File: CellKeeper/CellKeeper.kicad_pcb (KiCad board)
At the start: 4 copper layers, 260 x 113 mm, 470 parts, among them J1 Screw_Terminal_01x04, J10 3.81P Screw Terminal, J11 USB_C_Receptacle_USB2.0_16P, J12 Conn_02x10_Odd_Even, J14 ZE05H-8DP-2H, J15 Screw_Terminal_01x04, J16 Conn_01x03, J17 OEM HV Sense Connector, J18 7.62mm Pitch Screw Terminal, J19 USB_C_Receptacle_USB2.0_16P, J2 Screw_Terminal_01x01, J20 OEM Connector, J21 3.81P Screw Terminal, J22 Conn_02x10_Odd_Even, J3 Screw_Terminal_01x04, J4 8P8C_LED_Shielded_x2, J5 8P8C_LED_Shielded_x2, J6 S44B-RAD1AK, J7 Screw_Terminal_01x04, J8 Conn_01x03, J9 USB_C_Receptacle_USB2.0_16P, Q1 BSC0805LS, Q2 BSC0805LS, Q3 BSC0805LS, Q4 BSC0805LS, SW1 TS-1187A-B-A-B, SW2 TS-1187A-B-A-B, SW3 TS-1187A-B-A-B, SW4 TS-1187A-B-A-B, U1 UCC27524DR, U10 ISO1050DUB, U11 UCC27524DR, U12 LTV-217-B-G, U13 LTV-217-B-G, U14 RP2354B, U15 F0505S-1WR3, U16 ISO1540, U17 INA228, U18 ADS1115, U19 ADS1115, U20 RP2354B, U21 SP3485EN-L/TR, U22 AM26LV32EIDR, U25 TLV1117LV33DCYR, U26 TLV1117LV33DCYR, U3 TPS5430DDAR, U4 F0505S-1WR3, U5 ISO1050DUB, U6 LTV-217-B-G, U7 LTV-217-B-G, U8 LTV-217-B-G, U9 LTV-217-B-G, Y1 ABM8-272-T3, Y2 ABM8-272-T3

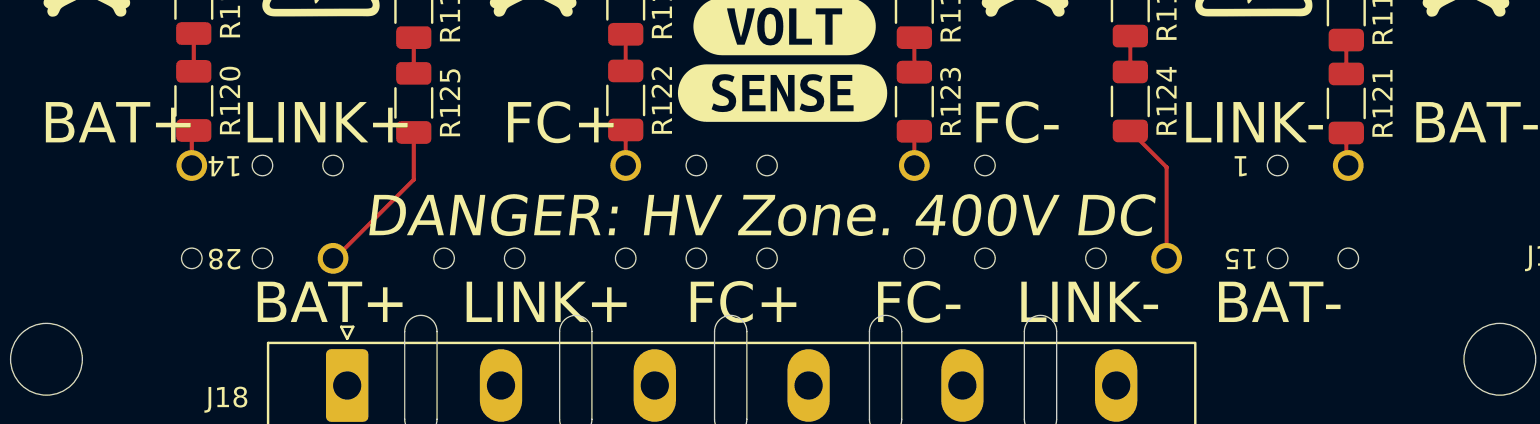
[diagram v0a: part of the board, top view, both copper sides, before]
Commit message: Update Symbol HV Sense
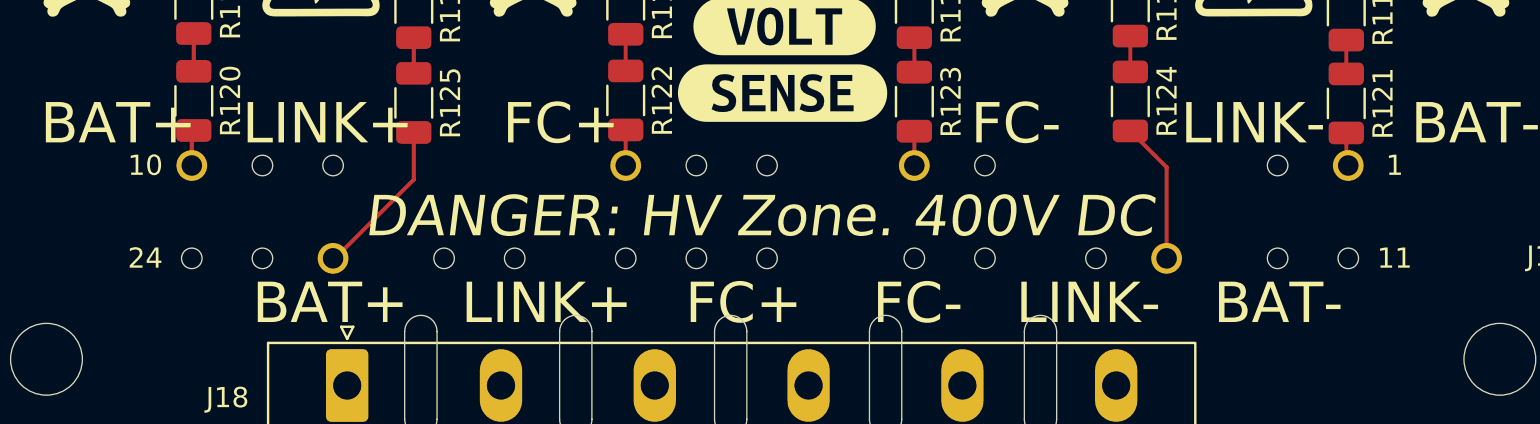
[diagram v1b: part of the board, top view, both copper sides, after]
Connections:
- J17 pad 1: Batt Positive -> Batt Negative
- J17 pad 10: Batt Negative -> Batt Positive
- J17 pad 13: Link Positive -> Link Negative
- J17 pad 22: Link Negative -> Link Positive
- J17 pad 4: FC Positive -> FC Negative
- J17 pad 7: FC Negative -> FC Positive
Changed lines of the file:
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@@
 			)
 		)
-		(property "Description" "Generic connector, single row, 01x24, script generated (kicad-library-utils/schlib/autogen/connector/)"
+		(property "Description" "TE 070 Multilock 24-position right-angle PCB header, TE circuit numbering, pins drawn as on the PCB"
 			(at 0 0 180)
 			(layer "F.Fab")
@@
 			(layer "F.Fab")
 		)
-		(fp_text user "14"
-			(at 4.768898 4.600001 180)
-			(unlocked yes)
-			(layer "F.SilkS")
-			(effects
-				(font
-					(size 1 1)
-					(thickness 0.15)
-				)
-			)
-		)
-		(fp_text user "28"
-			(at 4.768898 0 180)
+		(fp_text user "10"
+			(at 8.7019 4.6 0)
+			(unlocked yes)
+			(layer "F.SilkS")
+			(effects
+				(font
+					(size 1 1)
+					(thickness 0.15)
+				)
+			)
+		)
+		(fp_text user "24"
+			(at 8.7019 0 0)
 			(unlocked yes)
 			(layer "F.SilkS")
@@
 		)
 		(fp_text user "1"
-			(at -45.578298 4.600001 180)
-			(unlocked yes)
-			(layer "F.SilkS")
-			(effects
-				(font
-					(size 1 1)
-					(thickness 0.15)
-				)
-			)
-		)
-		(fp_text user "15"
-			(at -45.578298 0 180)
-			(unlocked yes)
-			(layer "F.SilkS")
-			(effects
-				(font
-					(size 1 1)
-					(thickness 0.15)
-				)
-			)
-		)
-		(fp_text user "14"
-			(at 4.768898 4.600001 0)
+			(at -53.1981 4.6 0)
+			(unlocked yes)
+			(layer "F.SilkS")
+			(effects
+				(font
+					(size 1 1)
+					(thickness 0.15)
+				)
+			)
+		)
+		(fp_text user "11"
+			(at -53.1981 0 0)
+			(unlocked yes)
+			(layer "F.SilkS")
+			(effects
+				(font
+					(size 1 1)
+					(thickness 0.15)
+				)
+			)
+		)
+		(fp_text user "10"
+			(at 8.7019 4.6 0)
 			(unlocked yes)
 			(layer "B.SilkS")
@@
 			)
 		)
-		(fp_text user "28"
-			(at 4.768898 0 0)
+		(fp_text user "24"
+			(at 8.7019 0 0)
 			(unlocked yes)
 			(layer "B.SilkS")
@@
 		)
 		(fp_text user "1"
-			(at -45.578298 4.600001 0)
+			(at -53.1981 4.6 0)
 			(unlocked yes)
 			(layer "B.SilkS")
@@
 			)
 		)
-		(fp_text user "15"
-			(at -45.578298 0 0)
+		(fp_text user "11"
+			(at -53.1981 0 0)
 			(unlocked yes)
 			(layer "B.SilkS")
@@
 			)
 		)
-		(fp_text user "14"
-			(at 4.768898 4.600001 180)
-			(unlocked yes)
-			(layer "F.Fab")
-			(effects
-				(font
-					(size 1 1)
-					(thickness 0.15)
-				)
-			)
-		)
-		(fp_text user "28"
-			(at 4.768898 0 180)
+		(fp_text user "10"
+			(at 8.7019 4.6 0)
+			(unlocked yes)
+			(layer "F.Fab")
+			(effects
+				(font
+					(size 1 1)
+					(thickness 0.15)
+				)
+			)
+		)
+		(fp_text user "24"
+			(at 8.7019 0 0)
 			(unlocked yes)
 			(layer "F.Fab")
@@
 		)
 		(fp_text user "1"
-			(at -45.578298 4.600001 180)
-			(unlocked yes)
-			(layer "F.Fab")
-			(effects
-				(font
-					(size 1 1)
-					(thickness 0.15)
-				)
-			)
-		)
-		(fp_text user "15"
-			(at -45.578298 0 180)
+			(at -53.1981 4.6 0)
+			(unlocked yes)
+			(layer "F.Fab")
+			(effects
+				(font
+					(size 1 1)
+					(thickness 0.15)
+				)
+			)
+		)
+		(fp_text user "11"
+			(at -53.1981 0 0)
 			(unlocked yes)
 			(layer "F.Fab")
@@
 			(layers "*.Cu" "*.Mask")
 		)
+		(pad "10" thru_hole circle
+			(at 6.399322 4.600001 180)
+			(size 1.524 1.524)
+			(drill 1.016)
+			(layers "*.Cu" "*.Mask")
+			(remove_unused_layers no)
+			(net "Batt Positive")
+			(pintype "passive")
+		)
+		(pad "7" thru_hole circle
+			(at -15.1 4.600001 180)
+			(size 1.524 1.524)
+			(drill 1.016)
+			(layers "*.Cu" "*.Mask")
+			(remove_unused_layers no)
+			(net "FC Positive")
+			(pintype "passive")
+		)
+		(pad "4" thru_hole circle
+			(at -29.398782 4.600001 180)
+			(size 1.524 1.524)
+			(drill 1.016)
+			(layers "*.Cu" "*.Mask")
+			(remove_unused_layers no)
+			(net "FC Negative")
+			(pintype "passive")
+		)
 		(pad "1" thru_hole circle
-			(at 6.399322 4.600001 180)
-			(size 1.524 1.524)
-			(drill 1.016)
-			(layers "*.Cu" "*.Mask")
-			(remove_unused_layers no)
-			(net "Batt Positive")
-			(pinfunction "Pin_1_1")
-			(pintype "passive")
-		)
-		(pad "4" thru_hole circle
-			(at -15.1 4.600001 180)
-			(size 1.524 1.524)
-			(drill 1.016)
-			(layers "*.Cu" "*.Mask")
-			(remove_unused_layers no)
-			(net "FC Positive")
-			(pinfunction "Pin_4_4")
-			(pintype "passive")
-		)
-		(pad "7" thru_hole circle
-			(at -29.398782 4.600001 180)
-			(size 1.524 1.524)
-			(drill 1.016)
-			(layers "*.Cu" "*.Mask")
-			(remove_unused_layers no)
-			(net "FC Negative")
-			(pinfunction "Pin_7_7")
-			(pintype "passive")
-		)
-		(pad "10" thru_hole circle
 			(at -50.898104 4.600001 180)
 			(size 1.524 1.524)
@@
 			(remove_unused_layers no)
 			(net "Batt Negative")
-			(pinfunction "Pin_10_10")
+			(pintype "passive")
+		)
+		(pad "22" thru_hole circle
+			(at -0.60041 0 180)
+			(size 1.524 1.524)
+			(drill 1.016)
+			(layers "*.Cu" "*.Mask")
+			(remove_unused_layers no)
+			(net "Link Positive")
 			(pintype "passive")
 		)
 		(pad "13" thru_hole circle
-			(at -0.60041 0 180)
-			(size 1.524 1.524)
-			(drill 1.016)
-			(layers "*.Cu" "*.Mask")
-			(remove_unused_layers no)
-			(net "Link Positive")
-			(pinfunction "Pin_13_13")
-			(pintype "passive")
-		)
-		(pad "22" thru_hole circle
 			(at -41.898376 0 180)
 			(size 1.524 1.524)
@@
 			(remove_unused_layers no)
 			(net "Link Negative")
-			(pinfunction "Pin_22_22")
-			(pintype "passive")
-		)
+			(pintype "passive")
+		)
